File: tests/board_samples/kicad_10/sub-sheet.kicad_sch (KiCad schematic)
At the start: 1 part, among them U1 74LS04

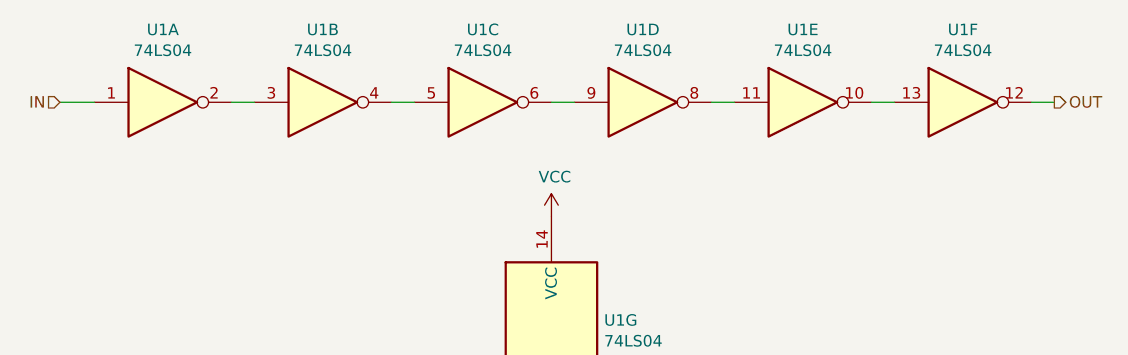
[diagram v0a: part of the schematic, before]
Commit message: [Schematic][Added] Support for private texts on symbols
- Introduced in KiCad 9
- Not documented, as usual
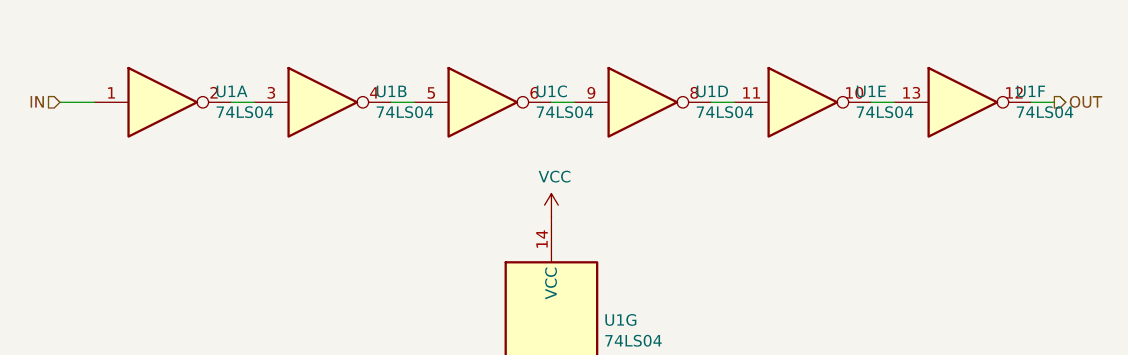
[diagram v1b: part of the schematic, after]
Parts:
- U1: private (none) -> PrivateField
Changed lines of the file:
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@@
 (kicad_sch
-	(version 20260101)
+	(version 20260306)
 	(generator "eeschema")
 	(generator_version "10.0")
@@
 	)
 	(symbol
+		(lib_name "74LS04_1")
 		(lib_id "74xx:74LS04")
 		(at 96.52 63.5 0)
@@
 		(dnp no)
 		(property "Reference" "U1"
-			(at 96.52 55.4482 0)
-			(show_name no)
-			(do_not_autoplace no)
-			(effects
-				(font
-					(size 1.27 1.27)
-				)
+			(at 102.362 62.3316 0)
+			(show_name no)
+			(do_not_autoplace no)
+			(effects
+				(font
+					(size 1.27 1.27)
+				)
+				(justify left)
 			)
 		)
 		(property "Value" "74LS04"
-			(at 96.52 57.7596 0)
-			(show_name no)
-			(do_not_autoplace no)
-			(effects
-				(font
-					(size 1.27 1.27)
-				)
+			(at 102.362 64.643 0)
+			(show_name no)
+			(do_not_autoplace no)
+			(effects
+				(font
+					(size 1.27 1.27)
+				)
+				(justify left)
 			)
 		)
@@
 		)
 		(property "Description" ""
+			(at 96.52 63.5 0)
+			(hide yes)
+			(show_name no)
+			(do_not_autoplace no)
+			(effects
+				(font
+					(size 1.27 1.27)
+				)
+			)
+		)
+		(property private "PrivateField" "Testing 1 2 3"
 			(at 96.52 63.5 0)
 			(hide yes)
@@
 	)
 	(symbol
+		(lib_name "74LS04_2")
 		(lib_id "74xx:74LS04")
 		(at 114.3 63.5 0)
@@
 		(dnp no)
 		(property "Reference" "U1"
-			(at 114.3 55.4482 0)
-			(show_name no)
-			(do_not_autoplace no)
-			(effects
-				(font
-					(size 1.27 1.27)
-				)
+			(at 120.142 62.3316 0)
+			(show_name no)
+			(do_not_autoplace no)
+			(effects
+				(font
+					(size 1.27 1.27)
+				)
+				(justify left)
 			)
 		)
 		(property "Value" "74LS04"
-			(at 114.3 57.7596 0)
-			(show_name no)
-			(do_not_autoplace no)
-			(effects
-				(font
-					(size 1.27 1.27)
-				)
+			(at 120.142 64.643 0)
+			(show_name no)
+			(do_not_autoplace no)
+			(effects
+				(font
+					(size 1.27 1.27)
+				)
+				(justify left)
 			)
 		)
@@
 		)
 		(property "Description" ""
+			(at 114.3 63.5 0)
+			(hide yes)
+			(show_name no)
+			(do_not_autoplace no)
+			(effects
+				(font
+					(size 1.27 1.27)
+				)
+			)
+		)
+		(property private "PrivateField" "Testing 1 2 3"
 			(at 114.3 63.5 0)
 			(hide yes)
@@
 	)
 	(symbol
+		(lib_name "74LS04_3")
 		(lib_id "74xx:74LS04")
 		(at 132.08 63.5 0)
@@
 		(dnp no)
 		(property "Reference" "U1"
-			(at 132.08 55.4482 0)
-			(show_name no)
-			(do_not_autoplace no)
-			(effects
-				(font
-					(size 1.27 1.27)
-				)
+			(at 137.922 62.3316 0)
+			(show_name no)
+			(do_not_autoplace no)
+			(effects
+				(font
+					(size 1.27 1.27)
+				)
+				(justify left)
 			)
 		)
 		(property "Value" "74LS04"
-			(at 132.08 57.7596 0)
-			(show_name no)
-			(do_not_autoplace no)
-			(effects
-				(font
-					(size 1.27 1.27)
-				)
+			(at 137.922 64.643 0)
+			(show_name no)
+			(do_not_autoplace no)
+			(effects
+				(font
+					(size 1.27 1.27)
+				)
+				(justify left)
 			)
 		)
@@
 		)
 		(property "Description" ""
+			(at 132.08 63.5 0)
+			(hide yes)
+			(show_name no)
+			(do_not_autoplace no)
+			(effects
+				(font
+					(size 1.27 1.27)
+				)
+			)
+		)
+		(property private "PrivateField" "Testing 1 2 3"
 			(at 132.08 63.5 0)
 			(hide yes)
@@
 	)
 	(symbol
+		(lib_name "74LS04_6")
 		(lib_id "74xx:74LS04")
 		(at 149.86 63.5 0)
@@
 		(dnp no)
 		(property "Reference" "U1"
-			(at 149.86 55.4482 0)
-			(show_name no)
-			(do_not_autoplace no)
-			(effects
-				(font
-					(size 1.27 1.27)
-				)
+			(at 155.702 62.3316 0)
+			(show_name no)
+			(do_not_autoplace no)
+			(effects
+				(font
+					(size 1.27 1.27)
+				)
+				(justify left)
 			)
 		)
 		(property "Value" "74LS04"
-			(at 149.86 57.7596 0)
-			(show_name no)
-			(do_not_autoplace no)
-			(effects
-				(font
-					(size 1.27 1.27)
-				)
+			(at 155.702 64.643 0)
+			(show_name no)
+			(do_not_autoplace no)
+			(effects
+				(font
+					(size 1.27 1.27)
+				)
+				(justify left)
 			)
 		)
@@
 		)
 		(property "Description" ""
+			(at 149.86 63.5 0)
+			(hide yes)
+			(show_name no)
+			(do_not_autoplace no)
+			(effects
+				(font
+					(size 1.27 1.27)
+				)
+			)
+		)
+		(property private "PrivateField" "Testing 1 2 3"
 			(at 149.86 63.5 0)
 			(hide yes)
@@
 	)
 	(symbol
+		(lib_name "74LS04_5")
 		(lib_id "74xx:74LS04")
 		(at 167.64 63.5 0)
@@
 		(dnp no)
 		(property "Reference" "U1"
-			(at 167.64 55.4482 0)
-			(show_name no)
-			(do_not_autoplace no)
-			(effects
-				(font
-					(size 1.27 1.27)
-				)
+			(at 173.482 62.3316 0)
+			(show_name no)
+			(do_not_autoplace no)
+			(effects
+				(font
+					(size 1.27 1.27)
+				)
+				(justify left)
 			)
 		)
 		(property "Value" "74LS04"
-			(at 167.64 57.7596 0)
-			(show_name no)
-			(do_not_autoplace no)
-			(effects
-				(font
-					(size 1.27 1.27)
-				)
+			(at 173.482 64.643 0)
+			(show_name no)
+			(do_not_autoplace no)
+			(effects
+				(font
+					(size 1.27 1.27)
+				)
+				(justify left)
 			)
 		)
@@
 		)
 		(property "Description" ""
+			(at 167.64 63.5 0)
+			(hide yes)
+			(show_name no)
+			(do_not_autoplace no)
+			(effects
+				(font
+					(size 1.27 1.27)
+				)
+			)
+		)
+		(property private "PrivateField" "Testing 1 2 3"
 			(at 167.64 63.5 0)
 			(hide yes)
@@
 	)
 	(symbol
+		(lib_name "74LS04_4")
 		(lib_id "74xx:74LS04")
 		(at 185.42 63.5 0)
@@
 		(dnp no)
 		(property "Reference" "U1"
-			(at 185.42 55.4482 0)
-			(show_name no)
-			(do_not_autoplace no)
-			(effects
-				(font
-					(size 1.27 1.27)
-				)
+			(at 191.262 62.3316 0)
+			(show_name no)
+			(do_not_autoplace no)
+			(effects
+				(font
+					(size 1.27 1.27)
+				)
+				(justify left)
 			)
 		)
 		(property "Value" "74LS04"
-			(at 185.42 57.7596 0)
-			(show_name no)
-			(do_not_autoplace no)
-			(effects
-				(font
-					(size 1.27 1.27)
-				)
+			(at 191.262 64.643 0)
+			(show_name no)
+			(do_not_autoplace no)
+			(effects
+				(font
+					(size 1.27 1.27)
+				)
+				(justify left)
 			)
 		)
@@
 		)
 		(property "Description" ""
+			(at 185.42 63.5 0)
+			(hide yes)
+			(show_name no)
+			(do_not_autoplace no)
+			(effects
+				(font
+					(size 1.27 1.27)
+				)
+			)
+		)
+		(property private "PrivateField" "Testing 1 2 3"
 			(at 185.42 63.5 0)
 			(hide yes)
@@
 			(at 139.7 88.9 0)
 			(hide yes)
+			(show_name no)
+			(do_not_autoplace no)
+			(effects
+				(font
+					(size 1.27 1.27)
+				)
+			)
+		)
+		(property private "PrivateField" "Testing 1 2 3"
+			(at 139.7 88.9 0)
+			(hide yes)
